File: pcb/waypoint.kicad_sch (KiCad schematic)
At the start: 4 parts, among them U1 ESP32-C6-WROOM-1-N8, U22 240x240 SPI

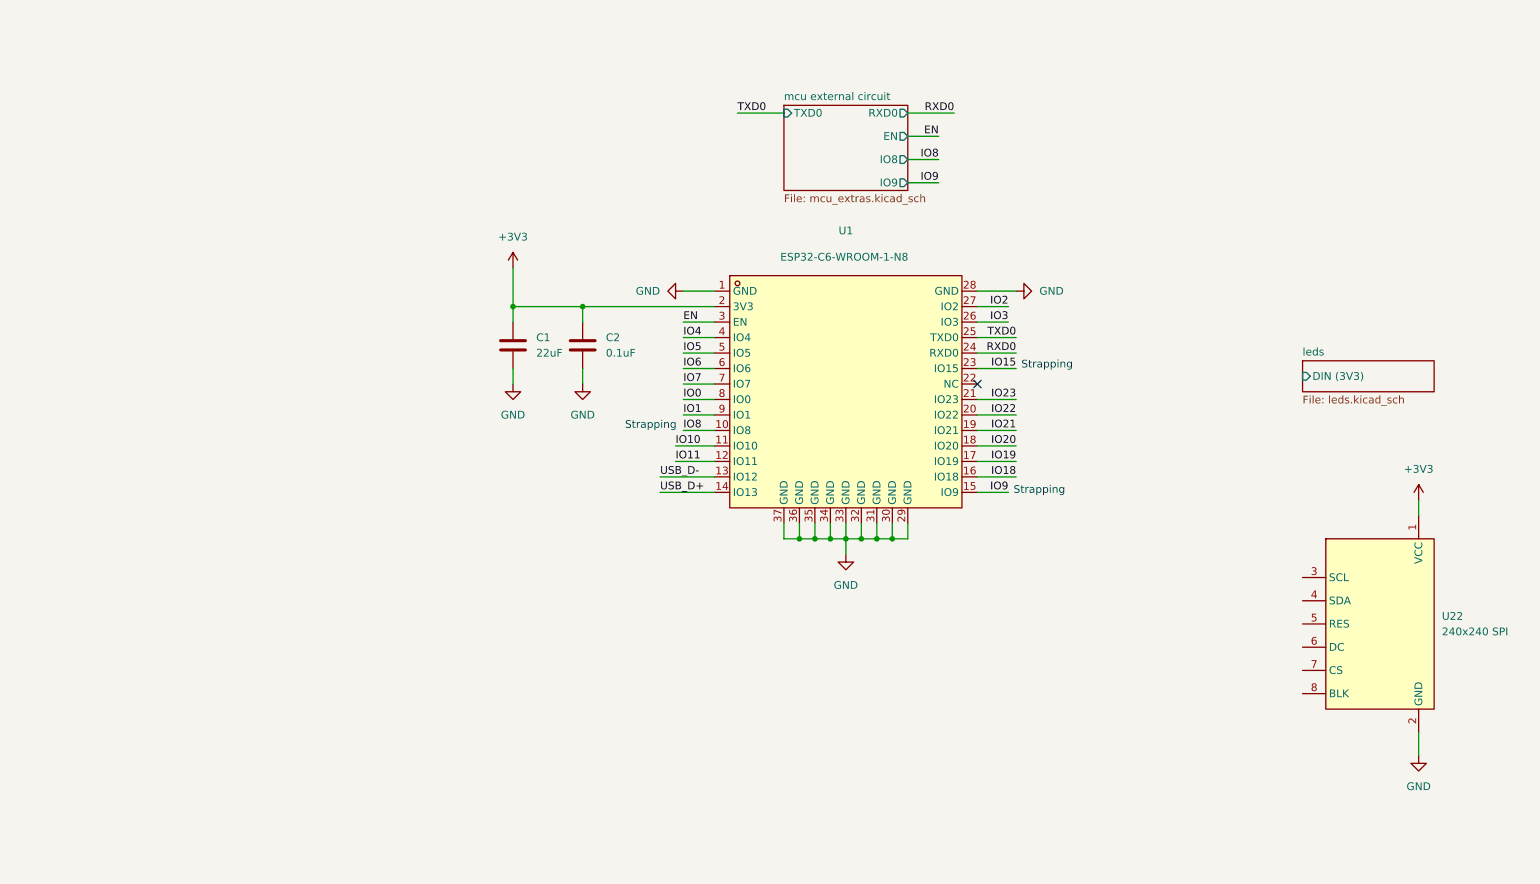
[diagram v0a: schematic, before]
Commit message: Added screen with footprint, started to add gps and imu
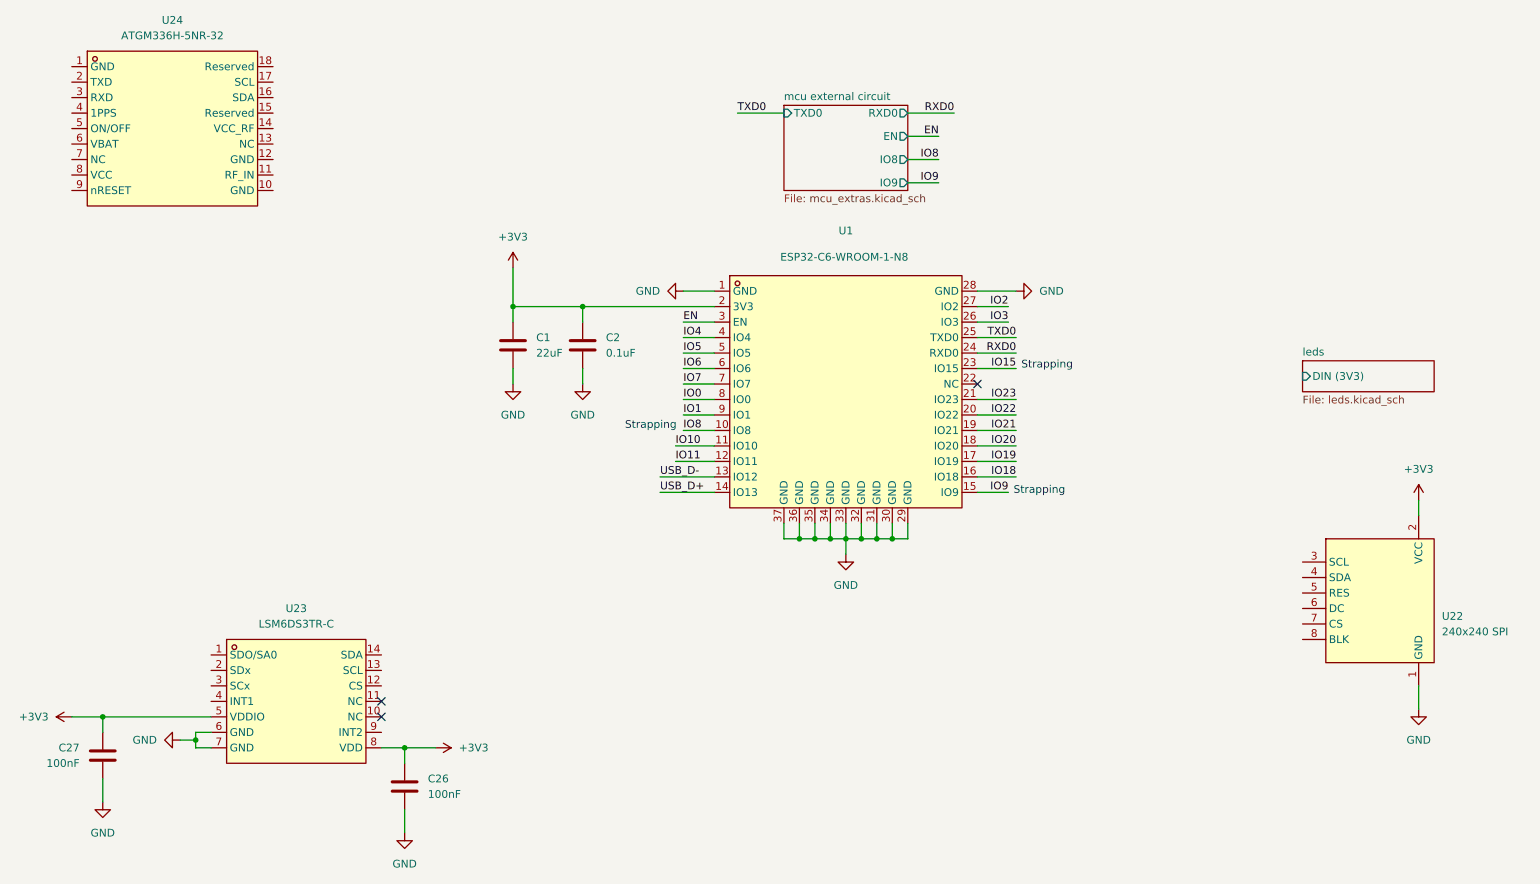
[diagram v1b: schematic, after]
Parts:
- added C26, C27: 100nF, symbol Device:C
- added U23: LSM6DS3TR-C, lcsc_lib:LGA-14_L3.0-W2.5-P0.50-TL, symbol lcsc:LSM6DS3TR-C
- added U24: ATGM336H-5NR-32, lcsc_lib:GPS-SMD_18P-L10.1-W9.7-P1.10-TL, symbol lcsc:ATGM336H-5NR-32
- U22: footprint (none) -> aliexpress:GC9A01; Link (none) -> https://de.aliexpress.com/item/1005010527932589.html
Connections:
- net +3V3: now also U22.2 (VCC), C26.1, C27.1, U23.5 (VDDIO), U23.8 (VDD); no longer U22.1 (VCC)
- net GND: now also U22.1 (GND), C26.2, C27.2, U23.6 (GND), U23.7 (GND); no longer U22.2 (GND)
- no-connect marks 1 -> 3
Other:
- moved on the sheet: U22

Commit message: Added GNSS, vibration with LRA and Power: Charging, LDO for GNSS, buck for main 3v3 and boost for led 5v
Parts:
- added AE1: Antenna, symbol Device:Antenna
- added C28: 220nF, symbol Device:C
- added C29, C30: 100nF, symbol Device:C
- added C31: 10uF, symbol Device:C
- added C42, C43: 1uF, symbol Device:C
- added J2: Conn_Coaxial, symbol Connector:Conn_Coaxial
- added L1: 47nH, symbol Device:L
- added M1: LD0832AA-0126F, lcsc_lib:MD-SMD_2P-LD0832AA-0126F, symbol lcsc:LD0832AA-0126F
- added R10: 0R, symbol Device:R
- added R11: 0R, Resistor_SMD:R_0603_1608Metric, symbol Device:R
- added R8, R9: 10kR, symbol Device:R
- added SW1: L, lcsc_lib:SW-SMD_L6.0-W6.0-LS6.6, symbol lcsc:TSB06341-050W811WA-R1000
- added SW2: OK, lcsc_lib:SW-SMD_L6.0-W6.0-LS6.6, symbol lcsc:TSB06341-050W811WA-R1000
- added SW3: R, lcsc_lib:SW-SMD_L6.0-W6.0-LS6.6, symbol lcsc:TSB06341-050W811WA-R1000
- added TP1: GPS_TX, symbol Connector:TestPoint
- added TP2: GPS_RX, symbol Connector:TestPoint
- added U25: IIS2MDCTR, lcsc_lib:LGA-12_L2.0-W2.0-P0.50-TL, symbol lcsc:IIS2MDCTR
- added U26: BX-PH2.0-2PWZ, lcsc_lib:CONN-TH_2P-P2.00_BX-PH2.0-2PWZ, symbol lcsc:BX-PH2.0-2PWZ
- added U31: DRV2605LDGST, lcsc_lib:VSSOP-10_L3.0-W3.0-P0.50-LS4.9-BL, symbol lcsc:DRV2605LDGST
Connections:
- net +3V3: now also U23.12 (CS), C29.1, C30.1, C31.1, C43.2, R8.1, R9.1, U25.10 (VDD_IO), U25.3 (CS), U25.9 (VDD), U31.10 (VDD), U31.5 (EN)
- net GND: now also U23.2 (SDx), U23.3 (SCx), U24.1 (GND), U24.10 (GND), U24.12 (GND), C28.2, C29.2, C30.2, C31.2, C42.1, C43.1, J2.2 (Ext), SW1.1, SW2.1, SW3.1, U25.11 (NC), U25.12 (NC), U25.2 (NC), U25.6 (GND), U25.8 (GND), U26.2, U31.4 (IN_TRIG), U31.8 (GND)
- net at U24.11 (RF_IN): now also L1.2, R10.1, R11.2
- net at U24.14 (VCC_RF): now also L1.1
- net at U24.2 (TXD): now also TP1.1
- net at U24.3 (RXD): now also TP2.1
- net +3.3VA: now reaches U24.6 (VBAT)
- net +3.3VA: now also U24.8 (VCC)
- new net: M1.1 (+), U31.7 (OUT+)
- new net: M1.2 (-), U31.9 (OUT-)
- new net: J2.1 (In), R11.1
- new net: C42.2, U31.1 (REG)
- new net: C28.1, U25.5 (C1)
- new net: AE1.1 (A), R10.2
- new net +BATT: U26.1
- no-connect marks 3 -> 13
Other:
- added sheet power (power.kicad_sch)
- note added: "0x5A"
- note added: "1.2mA"
- note added: "100mA"
- note added: "1mA"
- note added: "Controls"
- note added: "accelerometer + gyroscope"
- note added: "enable i2c"
- note added: "gps"
- note added: "magnetometer"
- moved on the sheet: C1, C2, C26, C27, U1, U22, U23, U24

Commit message: Finished schematic
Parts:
- removed AE1: Antenna, symbol Device:Antenna
- removed J2: Conn_Coaxial, symbol Connector:Conn_Coaxial
- removed R10: 0R, symbol Device:R
- removed R11: 0R, Resistor_SMD:R_0603_1608Metric, symbol Device:R
- added C10: 100nF, Capacitor_SMD:C_0603_1608Metric, symbol Device:C
- added C3: 1uF, Capacitor_SMD:C_0603_1608Metric, symbol Device:C
- added C6, C7: C, Capacitor_SMD:C_0603_1608Metric, symbol Device:C
- added L1: KH-GPS252504-WY, lcsc_lib:ANT-TH_KH-GPS252504-WY, symbol lcsc:KH-GPS252504-WY
- added R1, R4: 5.1kR, Resistor_SMD:R_0603_1608Metric, symbol Device:R
- added R12, R2, R5, R6, R7: 10kR, Resistor_SMD:R_0603_1608Metric, symbol Device:R
- added R3: 30kR, Resistor_SMD:R_0603_1608Metric, symbol Device:R
- added R8, R9: 22R, Resistor_SMD:R_0603_1608Metric, symbol Device:R
- added TP3: IO8, TestPoint:TestPoint_Loop_D2.50mm_Drill1.0mm, symbol Connector:TestPoint_Small
- added TP4: IO21, TestPoint:TestPoint_Loop_D2.50mm_Drill1.0mm, symbol Connector:TestPoint_Small
- added TP5: IO9, TestPoint:TestPoint_Loop_D2.50mm_Drill1.0mm, symbol Connector:TestPoint_Small
- added U10: TCA9534PWR, lcsc_lib:TSSOP-16_L5.0-W4.4-P0.65-LS6.4-BL, symbol lcsc:TCA9534PWR
- added U2: GT-USB-7010ASV, lcsc_lib:USB-C-SMD_G-SWITCH_GT-USB-7010ASV, symbol lcsc:GT-USB-7010ASV
- added U3: USBLC6-2SC6_C5261088, lcsc_lib:SOT-23-6_L2.9-W1.6-P0.95-LS2.8-BR, symbol lcsc:USBLC6-2SC6_C5261088
- C1: renamed from C43; footprint (none) -> Capacitor_SMD:C_0603_1608Metric; LCSC Part (none) -> C19702
- C11: renamed from C30; footprint (none) -> Capacitor_SMD:C_0603_1608Metric; LCSC Part (none) -> C14663
- C12: renamed from C29; footprint (none) -> Capacitor_SMD:C_0603_1608Metric; LCSC Part (none) -> C14663
- C13: renamed from C31; footprint (none) -> Capacitor_SMD:C_0603_1608Metric; LCSC Part (none) -> C96446
- C14: renamed from C28; footprint (none) -> Capacitor_SMD:C_0603_1608Metric; LCSC Part (none) -> C107083
- C2: renamed from C42; footprint (none) -> Capacitor_SMD:C_0603_1608Metric; LCSC Part (none) -> C19702
- C4: renamed from C1; LCSC Part (none) -> C86295
- C5: renamed from C2; value 0.1uF -> 100nF; LCSC Part (none) -> C14663
- C8: renamed from C27; footprint (none) -> Capacitor_SMD:C_0603_1608Metric; LCSC Part (none) -> C14663
- C9: renamed from C26; footprint (none) -> Capacitor_SMD:C_0603_1608Metric; LCSC Part (none) -> C14663
- L2: renamed from L1; footprint (none) -> Inductor_SMD:L_0603_1608Metric; LCSC Part (none) -> C6807998
- R10: renamed from R8; value 10kR -> 2.2kR; footprint (none) -> Resistor_SMD:R_0603_1608Metric; LCSC Part (none) -> C2907005
- R11: renamed from R9; value 10kR -> 2.2kR; footprint (none) -> Resistor_SMD:R_0603_1608Metric; LCSC Part (none) -> C2907005
- TP1, TP2: footprint (none) -> TestPoint:TestPoint_Loop_D2.50mm_Drill1.0mm
- renumbered U26 to U1, U31 to U4, U1 to U5, U22 to U6, U24 to U7, U23 to U8, U25 to U9
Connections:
- net IO10 is gone; now on net SCL: U5.11 (IO10)
- net IO11 is gone; now on net SDA: U5.12 (IO11)
- net IO18 is gone; now on net RXD1: U5.16 (IO18)
- net IO19 is gone; now on net TXD1: U5.17 (IO19)
- net IO2 is gone; now on net RESET: U5.27 (IO2)
- net IO20 is gone; now on net CS: U5.18 (IO20)
- net IO21 is gone; now on net DC: U5.19 (IO21)
- net IO22 is gone; now on net BLK: U5.20 (IO22)
- net IO6 is gone; now on net SCLK: U5.6 (IO6)
- net IO7 is gone; now on net MOSI: U5.7 (IO7)
- net +3V3: now also C10.1, R12.1, R5.2, R6.2, R7.2, U10.16 (VCC)
- net +BATT: now also R2.1
- net GND: now also U8.1 (SDO/SA0), U8.9 (INT2), C10.2, C3.2, C6.2, C7.2, R1.1, R3.2, R4.1, U10.1 (A0), U10.2 (A1), U10.3 (A2), U10.8 (GND), U2.1 (SHELL), U2.2 (SHELL), U2.3 (SHELL), U2.4 (SHELL), U2.A1B12 (GND), U2.B1A12 (GND), U3.2
- net USB_D+: now also R9.1, U2.A6 (DP1), U2.B6 (DP2), U3.1, U3.6; no longer U5.14 (IO13)
- net USB_D-: now also R8.1, U2.A7 (DN1), U2.B7 (DN2), U3.3, U3.4; no longer U5.13 (IO12)
- net at L2.2, U7.11 (RF_IN): now also L1.1 (ANT)
- net RXD1: now reaches TP1.1, U7.2 (TXD)
- net TXD1: now reaches TP2.1, U7.3 (RXD)
- net GNSS_ON: now reaches U7.5 (ON/OFF)
- net GNSS_ON: now also U10.10 (P5)
- net OK_SW: now reaches SW2.2
- net OK_SW: now also R6.1, U10.7 (P3)
- net SCL: now reaches U8.13 (SCL)
- net SCL: now also R10.2, U4.2 (SCL), U9.1 (SCL/SPC), U10.14 (SCL)
- net SDA: now reaches U8.14 (SDA)
- net SDA: now also R11.2, U4.3 (SDA), U9.4 (SDA/SDI/SDO), U10.15 (SDA)
- net IMU_INT: now reaches U8.4 (INT1)
- net IMU_INT: now also U10.9 (P4)
- net SCLK: now reaches U6.3 (SCL)
- net MOSI: now reaches U6.4 (SDA)
- net RESET: now reaches U6.5 (RES)
- net DC: now reaches U6.6 (DC)
- net DC: now also TP4.1
- net CS: now reaches U6.7 (CS)
- net BLK: now reaches U6.8 (BLK)
- net R_SW: now reaches SW3.2
- net R_SW: now also R7.1, U10.12 (P7)
- net L_SW: now reaches SW1.2
- net L_SW: now also R5.1, U10.6 (P2)
- net IO0 renamed LED_EN
- net IO1 renamed BATT_SENSE
- net BATT_SENSE: now also C3.1, R2.2, R3.1
- net IO15: no longer names the net of U5.23 (IO15)
- net IO23 renamed LED_DATA
- net IO3 renamed EXPANDER_INT
- net EXPANDER_INT: now also R12.2, U10.13 (~{INT})
- net IO4: no longer names the net of U5.4 (IO4)
- net IO5: no longer names the net of U5.5 (IO5)
- net IO8 renamed GNSS_EN
- net GNSS_EN: now also TP3.1
- net IO9 renamed MAIN_EN
- net MAIN_EN: now also TP5.1
- new net: C6.1, R8.2, U5.13 (IO12)
- new net: C7.1, R9.2, U5.14 (IO13)
- new net: R1.2, U2.A5 (CC1)
- new net: R4.2, U2.B5 (CC2)
- new net CHG: U10.5 (P1)
- new net PGOOD: U10.4 (P0)
- new net PWR_SW: U10.11 (P6)
- new net VBUS: U2.A4B9 (VBUS), U2.B4A9 (VBUS), U3.5
- no-connect marks 13 -> 18
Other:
- sheet leds ports: added DIN; removed DIN (3V3)
- sheet mcu external circuit ports: added none; removed IO8, IO9
- note added: "0x1E"
- note added: "0x20"
- note added: "0x6A"
- note added: "Battery + Power"
- note added: "GNSS"
- note added: "Haptics"
- note added: "I/O Expander"
- note added: "LEDS"
- note added: "Note uncommon pin labels for QSPI"
- note added: "Screen"
- note added: "Strapping (any)"
- note added: "Strapping (high)"
- note added: "USB"
- note removed: "1.2mA"
- note removed: "100mA"
- note removed: "1mA"
- note removed: "gps"
- moved on the sheet: C1, C11, C12, C13, C14, C2, C4, C5, C8, C9, L2, M1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

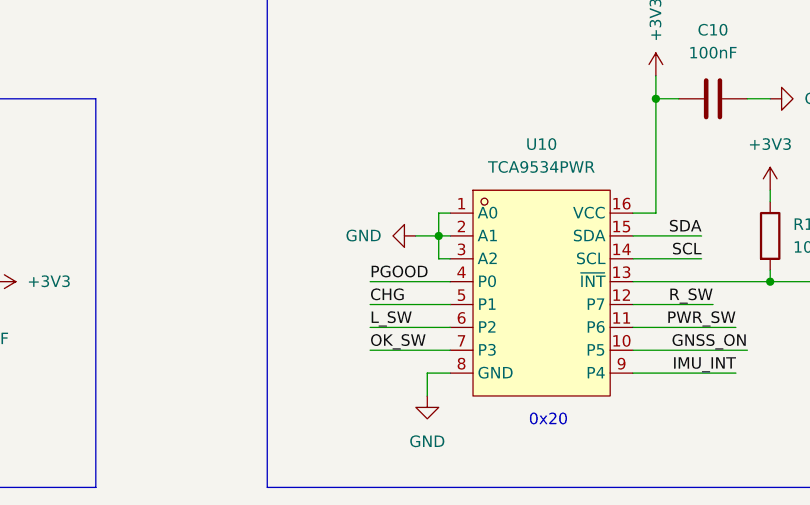
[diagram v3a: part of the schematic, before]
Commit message: Finished routing and added silkscreen art
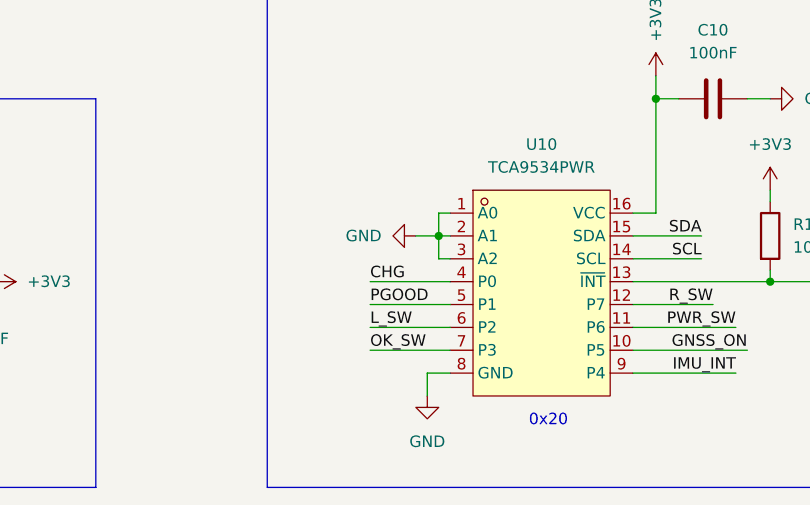
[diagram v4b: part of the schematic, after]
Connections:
- net CHG: now also U10.4 (P0); no longer U10.5 (P1)
- net PGOOD: now also U10.5 (P1); no longer U10.4 (P0)
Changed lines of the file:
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@@
+	(wire
+		(pts
+			(xy 190.5 241.3) (xy 199.39 241.3)
+		)
+		(stroke
+			(width 0)
+			(type default)
+		)
+	)
 	(wire
 		(pts
@@
 	(wire
 		(pts
+			(xy 190.5 243.84) (xy 199.39 243.84)
+		)
+		(stroke
+			(width 0)
+			(type default)
+		)
+	)
+	(wire
+		(pts
 			(xy 93.98 38.1) (xy 102.87 38.1)
 		)
@@
 	(wire
 		(pts
-			(xy 190.5 243.84) (xy 199.39 243.84)
-		)
-		(stroke
-			(width 0)
-			(type default)
-		)
-	)
-	(wire
-		(pts
 			(xy 81.28 196.85) (xy 86.36 196.85)
 		)
@@
 		(pts
 			(xy 198.12 139.7) (xy 193.04 139.7)
-		)
-		(stroke
-			(width 0)
-			(type default)
-		)
-	)
-	(wire
-		(pts
-			(xy 190.5 241.3) (xy 199.39 241.3)
 		)
 		(stroke
@@
 		)
 	)
+	(label "PGOOD"
+		(at 190.5 243.84 0)
+		(effects
+			(font
+				(size 1.27 1.27)
+			)
+			(justify left bottom)
+		)
+	)
 	(label "CHG"
 		(at 262.89 25.4 180)
@@
 		)
 	)
-	(label "CHG"
-		(at 190.5 243.84 0)
-		(effects
-			(font
-				(size 1.27 1.27)
-			)
-			(justify left bottom)
-		)
-	)
 	(label "RXD1"
 		(at 24.13 130.81 0)
@@
 		)
 	)
+	(label "CHG"
+		(at 190.5 241.3 0)
+		(effects
+			(font
+				(size 1.27 1.27)
+			)
+			(justify left bottom)
+		)
+	)
 	(label "GNSS_ON"
 		(at 30.48 138.43 0)
@@
 		(effects
 			(font
-				(size 1.27 1.27)
-			)
-			(justify left bottom)
-		)
-	)
-	(label "PGOOD"
-		(at 190.5 241.3 0)
-		(effects
-			(font
